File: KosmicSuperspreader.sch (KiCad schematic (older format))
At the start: 28 parts, among them J1 CV INPUT, J2 SPREAD INPUT, J3 OUT -, J4 OUT +, J5 BUFFER, J6 SYNTH POWER, U1 TL072, U2 TL074

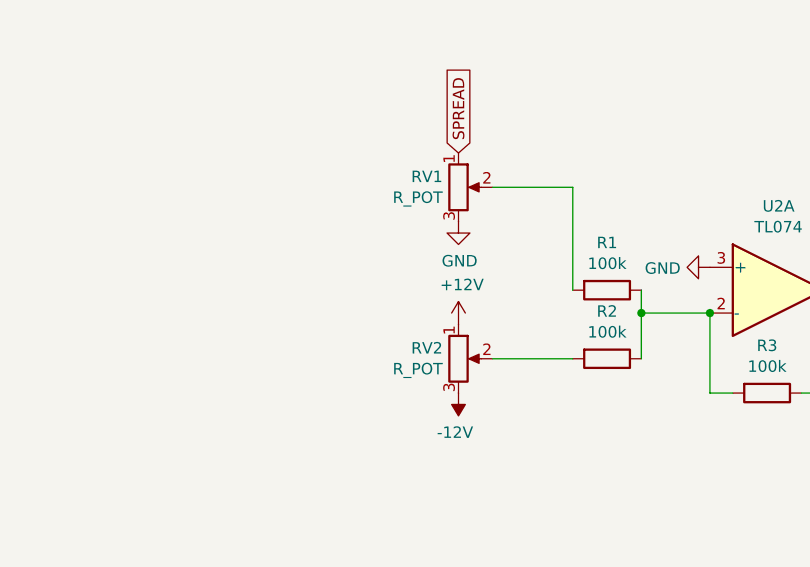
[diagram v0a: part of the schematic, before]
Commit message: Pot labels
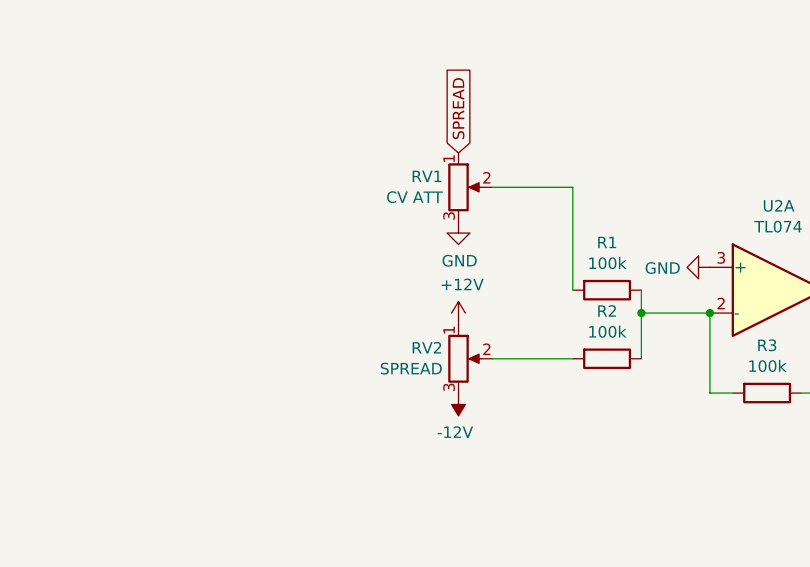
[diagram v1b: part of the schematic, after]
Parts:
- RV1: value R_POT -> CV ATT
- RV2: value R_POT -> SPREAD
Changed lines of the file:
@@
 P 3300 3700
 F 0 "RV2" H 3231 3746 50  0000 R CNN
-F 1 "R_POT" H 3231 3655 50  0000 R CNN
+F 1 "SPREAD" H 3231 3655 50  0000 R CNN
 F 2 "Sonosus:Potentiometer_Alpha_RD901F-40-00D" H 3300 3700 50  0001 C CNN
 F 3 "~" H 3300 3700 50  0001 C CNN
@@
 P 3300 2950
 F 0 "RV1" H 3231 2996 50  0000 R CNN
-F 1 "R_POT" H 3231 2905 50  0000 R CNN
+F 1 "CV ATT" H 3231 2905 50  0000 R CNN
 F 2 "Sonosus:Potentiometer_Alpha_RD901F-40-00D" H 3300 2950 50  0001 C CNN
 F 3 "~" H 3300 2950 50  0001 C CNN
